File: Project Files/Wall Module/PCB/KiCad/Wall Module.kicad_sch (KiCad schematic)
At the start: 15 parts, among them J1 Conn_02x03_Top_Bottom (C65114), J2 Screw_Terminal_01x04 (C280261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, K1 SANYOU_SRD_Form_C (C35449), K2 SANYOU_SRD_Form_C (C35449), Q1 MMBT3904 (C20526), Q2 MMBT3904 (C20526), U1 AMS1117-3.3 (C173386)

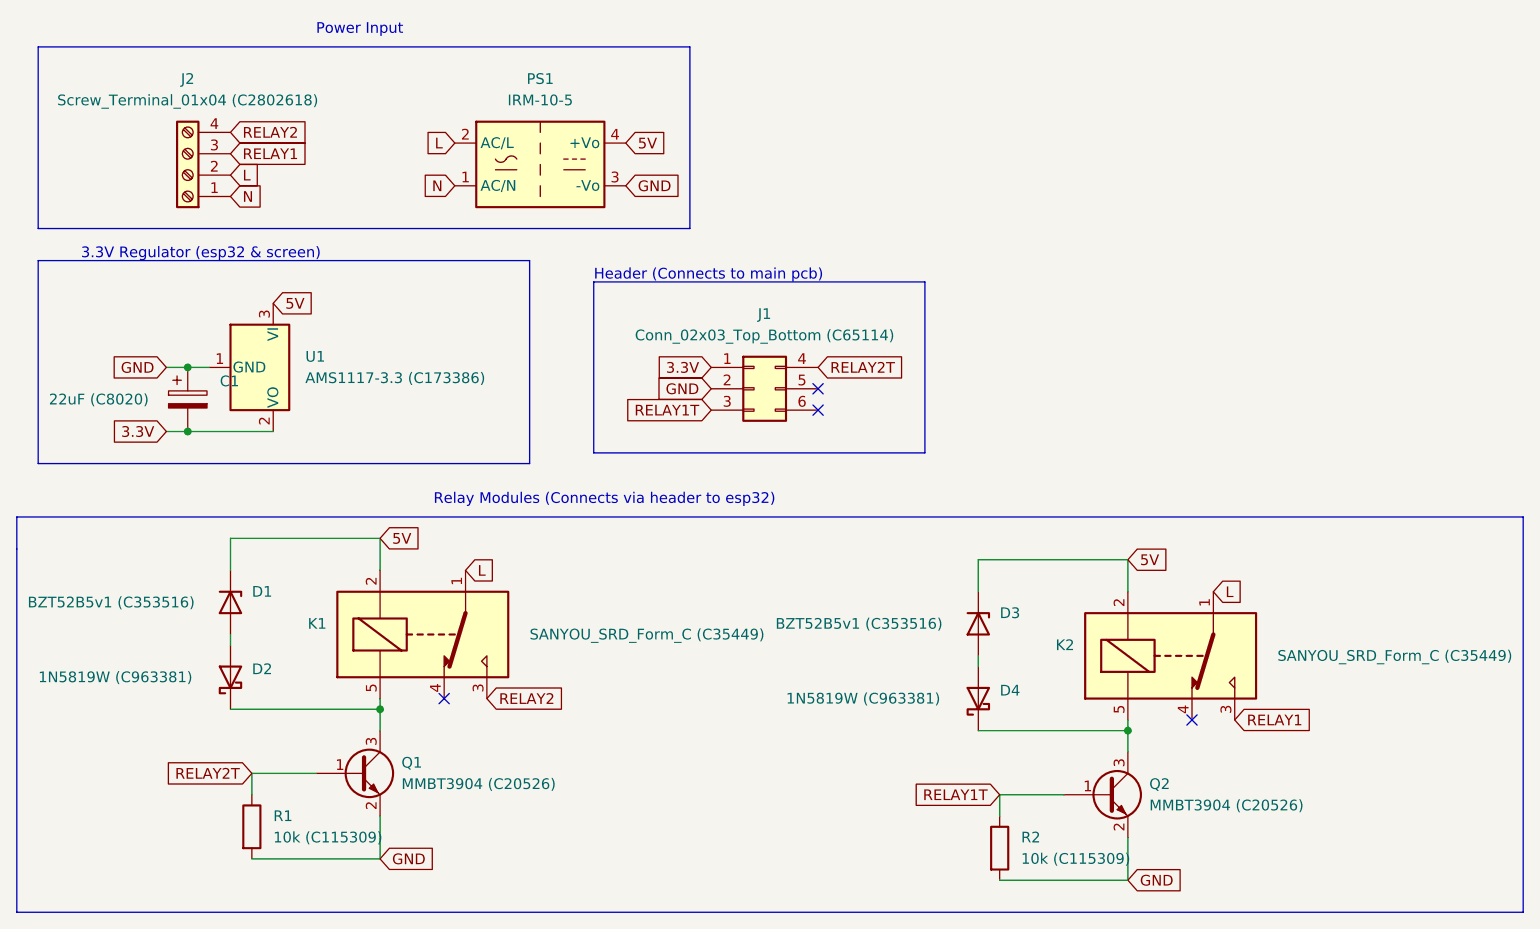
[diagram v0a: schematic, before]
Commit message: Updated PCB to fix several issues Wall Module: Fixed relay flyback diodes pointing in the wrong direction.
Screen PCB:
Fixed display LED resistors to be a more suitable value.
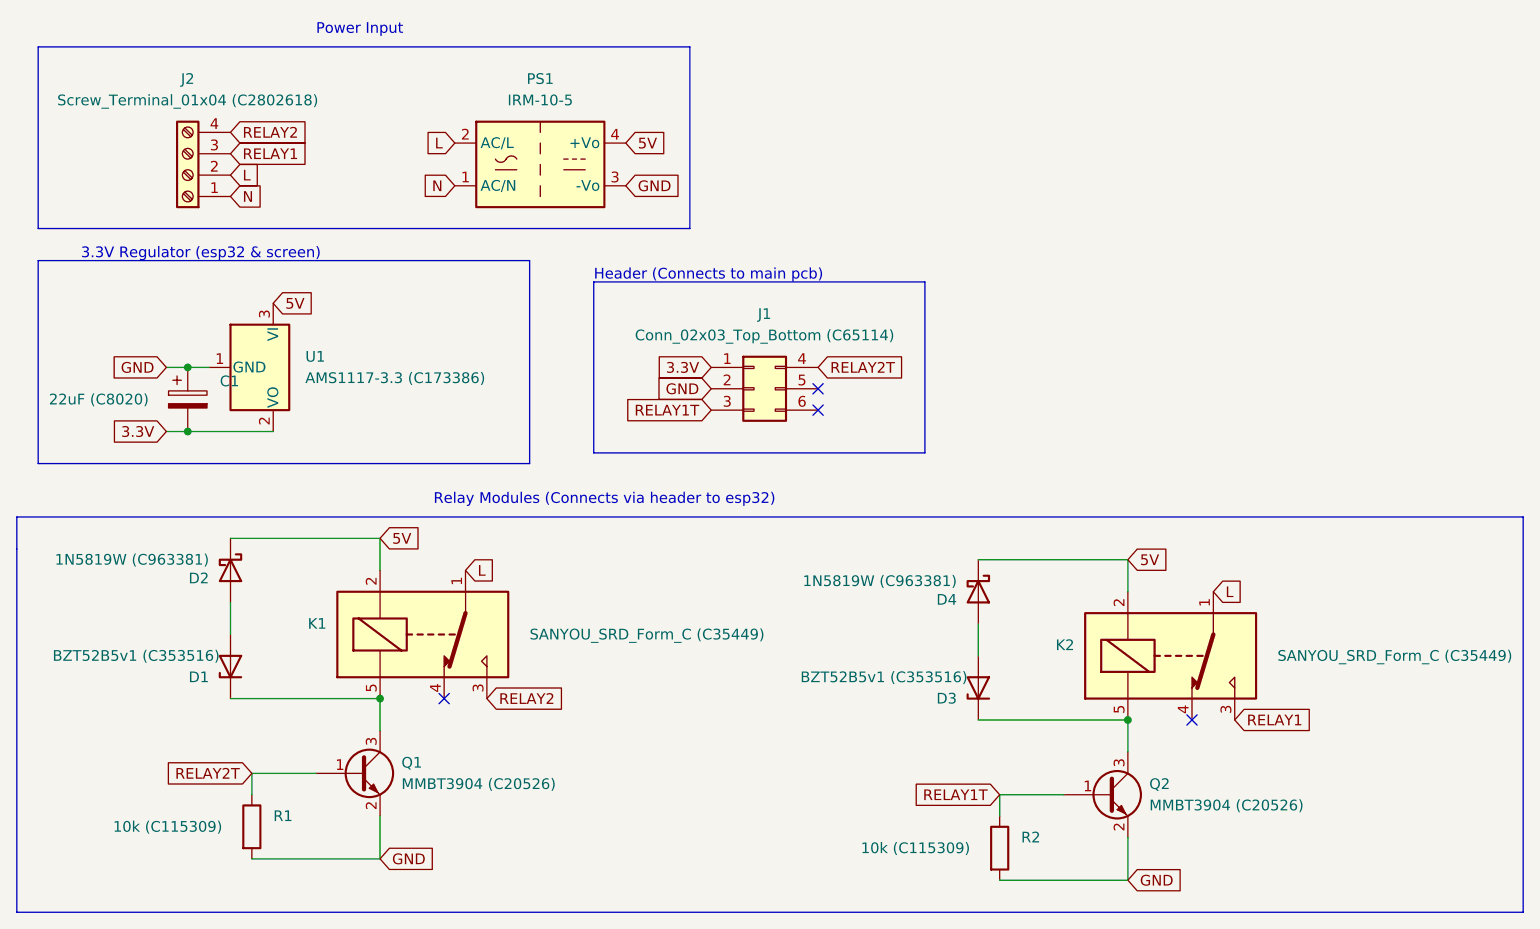
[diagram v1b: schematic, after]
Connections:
- net 5V: now also D2.1 (K), D4.1 (K); no longer D1.1 (K), D3.1 (K)
- net at K1.5, Q1.3 (C): now also D1.1 (K); no longer D2.1 (K)
- net at K2.5, Q2.3 (C): now also D3.1 (K); no longer D4.1 (K)
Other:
- moved on the sheet: D1, D2, D3, D4
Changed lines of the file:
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@@
 (kicad_sch (version 20211123) (generator eeschema)
   (paper "A4")
+  (junction (at 147.32 104.14) (diameter 0) (color 0 0 0 0)
+  )
+  (junction (at 58.42 101.6) (diameter 0) (color 0 0 0 0)
+  )
   (junction (at 35.56 69.85) (diameter 0) (color 0 0 0 0)
-  )
-  (junction (at 147.32 105.41) (diameter 0) (color 0 0 0 0)
-  )
-  (junction (at 58.42 102.87) (diameter 0) (color 0 0 0 0)
   )
   (junction (at 35.56 62.23) (diameter 0) (color 0 0 0 0)
@@
   (no_connect (at 66.04 101.6))
   (no_connect (at 110.49 64.77))
-  (wire (pts (xy 40.64 86.36) (xy 40.64 82.55))
-    (stroke (width 0) (type default) (color 0 0 0 0))
-  )
   (polyline (pts (xy 83.82 72.39) (xy 123.19 72.39))
     (stroke (width 0) (type default) (color 0 0 0 0))
@@
     (stroke (width 0) (type default) (color 0 0 0 0))
   )
-  (wire (pts (xy 147.32 105.41) (xy 147.32 104.14))
+  (wire (pts (xy 129.54 104.14) (xy 147.32 104.14))
+    (stroke (width 0) (type default) (color 0 0 0 0))
+  )
+  (wire (pts (xy 40.64 101.6) (xy 58.42 101.6))
     (stroke (width 0) (type default) (color 0 0 0 0))
   )
@@
     (stroke (width 0) (type default) (color 0 0 0 0))
   )
-  (wire (pts (xy 58.42 102.87) (xy 58.42 101.6))
-    (stroke (width 0) (type default) (color 0 0 0 0))
-  )
-  (wire (pts (xy 129.54 88.9) (xy 129.54 85.09))
+  (wire (pts (xy 58.42 101.6) (xy 58.42 105.41))
+    (stroke (width 0) (type default) (color 0 0 0 0))
+  )
+  (wire (pts (xy 40.64 90.17) (xy 40.64 93.98))
     (stroke (width 0) (type default) (color 0 0 0 0))
   )
@@
     (stroke (width 0) (type default) (color 0 0 0 0))
   )
-  (wire (pts (xy 58.42 105.41) (xy 58.42 102.87))
-    (stroke (width 0) (type default) (color 0 0 0 0))
-  )
   (wire (pts (xy 139.7 113.03) (xy 132.08 113.03))
     (stroke (width 0) (type default) (color 0 0 0 0))
@@
     (stroke (width 0) (type default) (color 0 0 0 0))
   )
+  (wire (pts (xy 129.54 92.71) (xy 129.54 96.52))
+    (stroke (width 0) (type default) (color 0 0 0 0))
+  )
   (polyline (pts (xy 15.24 127) (xy 194.31 127))
     (stroke (width 0) (type default) (color 0 0 0 0))
   )
-  (wire (pts (xy 147.32 107.95) (xy 147.32 105.41))
+  (wire (pts (xy 147.32 104.14) (xy 147.32 107.95))
     (stroke (width 0) (type default) (color 0 0 0 0))
   )
@@
     (stroke (width 0) (type default) (color 0 0 0 0))
   )
-  (wire (pts (xy 40.64 102.87) (xy 58.42 102.87))
-    (stroke (width 0) (type default) (color 0 0 0 0))
-  )
-  (wire (pts (xy 129.54 105.41) (xy 147.32 105.41))
-    (stroke (width 0) (type default) (color 0 0 0 0))
-  )
   (wire (pts (xy 43.18 120.65) (xy 58.42 120.65))
     (stroke (width 0) (type default) (color 0 0 0 0))
@@
     (stroke (width 0) (type default) (color 0 0 0 0))
   )
-  (wire (pts (xy 40.64 93.98) (xy 40.64 95.25))
-    (stroke (width 0) (type default) (color 0 0 0 0))
-  )
   (polyline (pts (xy 83.82 52.07) (xy 83.82 72.39))
     (stroke (width 0) (type default) (color 0 0 0 0))
@@
   )
   (polyline (pts (xy 194.31 80.01) (xy 15.24 80.01))
-    (stroke (width 0) (type default) (color 0 0 0 0))
-  )
-  (wire (pts (xy 129.54 96.52) (xy 129.54 97.79))
     (stroke (width 0) (type default) (color 0 0 0 0))
   )
@@
   )
   (symbol (lib_id "Device:R") (at 132.08 119.38 0) (unit 1)
-    (in_bom yes) (on_board yes) (fields_autoplaced)
+    (in_bom yes) (on_board yes)
     (property "Reference" "R2" (id 0) (at 134.62 118.1099 0)
       (effects (font (size 1.27 1.27)) (justify left))
     )
-    (property "Value" "10k (C115309)" (id 1) (at 134.62 120.6499 0)
+    (property "Value" "10k (C115309)" (id 1) (at 115.57 119.38 0)
       (effects (font (size 1.27 1.27)) (justify left))
     )
@@
   )
   (symbol (lib_id "Device:R") (at 43.18 116.84 0) (unit 1)
-    (in_bom yes) (on_board yes) (fields_autoplaced)
+    (in_bom yes) (on_board yes)
     (property "Reference" "R1" (id 0) (at 45.72 115.5699 0)
       (effects (font (size 1.27 1.27)) (justify left))
     )
-    (property "Value" "10k (C115309)" (id 1) (at 45.72 118.1099 0)
+    (property "Value" "10k (C115309)" (id 1) (at 26.67 116.84 0)
       (effects (font (size 1.27 1.27)) (justify left))
     )
@@
     (pin "2")
   )
-  (symbol (lib_id "Diode:1N5819") (at 40.64 99.06 90) (unit 1)
-    (in_bom yes) (on_board yes)
-    (property "Reference" "D2" (id 0) (at 43.18 98.1074 90)
-      (effects (font (size 1.27 1.27)) (justify right))
-    )
-    (property "Value" "1N5819W (C963381)" (id 1) (at 17.78 99.06 90)
-      (effects (font (size 1.27 1.27)) (justify right))
-    )
-    (property "Footprint" "Diode_SMD:D_SOD-123" (id 2) (at 45.085 99.06 0)
-      (effects (font (size 1.27 1.27)) hide)
-    )
-    (property "Datasheet" "http://www.vishay.com/docs/88525/1n5817.pdf" (id 3) (at 40.64 99.06 0)
+  (symbol (lib_id "Diode:1N5819") (at 40.64 86.36 270) (unit 1)
+    (in_bom yes) (on_board yes)
+    (property "Reference" "D2" (id 0) (at 38.1 87.3126 90)
+      (effects (font (size 1.27 1.27)) (justify right))
+    )
+    (property "Value" "1N5819W (C963381)" (id 1) (at 38.1 85.09 90)
+      (effects (font (size 1.27 1.27)) (justify right))
+    )
+    (property "Footprint" "Diode_SMD:D_SOD-123" (id 2) (at 36.195 86.36 0)
+      (effects (font (size 1.27 1.27)) hide)
+    )
+    (property "Datasheet" "http://www.vishay.com/docs/88525/1n5817.pdf" (id 3) (at 40.64 86.36 0)
       (effects (font (size 1.27 1.27)) hide)
     )
@@
     (pin "5")
   )
-  (symbol (lib_id "Diode:1N5819") (at 129.54 101.6 90) (unit 1)
-    (in_bom yes) (on_board yes)
-    (property "Reference" "D4" (id 0) (at 132.08 100.6474 90)
-      (effects (font (size 1.27 1.27)) (justify right))
-    )
-    (property "Value" "1N5819W (C963381)" (id 1) (at 106.68 101.6 90)
-      (effects (font (size 1.27 1.27)) (justify right))
-    )
-    (property "Footprint" "Diode_SMD:D_SOD-123" (id 2) (at 133.985 101.6 0)
-      (effects (font (size 1.27 1.27)) hide)
-    )
-    (property "Datasheet" "http://www.vishay.com/docs/88525/1n5817.pdf" (id 3) (at 129.54 101.6 0)
+  (symbol (lib_id "Diode:1N5819") (at 129.54 88.9 270) (unit 1)
+    (in_bom yes) (on_board yes)
+    (property "Reference" "D4" (id 0) (at 127 89.8526 90)
+      (effects (font (size 1.27 1.27)) (justify right))
+    )
+    (property "Value" "1N5819W (C963381)" (id 1) (at 127 87.63 90)
+      (effects (font (size 1.27 1.27)) (justify right))
+    )
+    (property "Footprint" "Diode_SMD:D_SOD-123" (id 2) (at 125.095 88.9 0)
+      (effects (font (size 1.27 1.27)) hide)
+    )
+    (property "Datasheet" "http://www.vishay.com/docs/88525/1n5817.pdf" (id 3) (at 129.54 88.9 0)
       (effects (font (size 1.27 1.27)) hide)
     )
@@
     (pin "6")
   )
-  (symbol (lib_id "Diode:BZT52Bxx") (at 40.64 90.17 270) (unit 1)
-    (in_bom yes) (on_board yes)
-    (property "Reference" "D1" (id 0) (at 43.18 88.8999 90)
-      (effects (font (size 1.27 1.27)) (justify left))
-    )
-    (property "Value" "BZT52B5v1 (C353516)" (id 1) (at 16.51 90.17 90)
-      (effects (font (size 1.27 1.27)) (justify left))
-    )
-    (property "Footprint" "Diode_SMD:D_SOD-123" (id 2) (at 36.195 90.17 0)
-      (effects (font (size 1.27 1.27)) hide)
-    )
-    (property "Datasheet" "https://diotec.com/tl_files/diotec/files/pdf/datasheets/bzt52b2v4.pdf" (id 3) (at 40.64 90.17 0)
+  (symbol (lib_id "Diode:BZT52Bxx") (at 40.64 97.79 90) (unit 1)
+    (in_bom yes) (on_board yes)
+    (property "Reference" "D1" (id 0) (at 38.1 99.0601 90)
+      (effects (font (size 1.27 1.27)) (justify left))
+    )
+    (property "Value" "BZT52B5v1 (C353516)" (id 1) (at 39.37 96.52 90)
+      (effects (font (size 1.27 1.27)) (justify left))
+    )
+    (property "Footprint" "Diode_SMD:D_SOD-123" (id 2) (at 45.085 97.79 0)
+      (effects (font (size 1.27 1.27)) hide)
+    )
+    (property "Datasheet" "https://diotec.com/tl_files/diotec/files/pdf/datasheets/bzt52b2v4.pdf" (id 3) (at 40.64 97.79 0)
       (effects (font (size 1.27 1.27)) hide)
     )
@@
     (pin "2")
   )
-  (symbol (lib_id "Diode:BZT52Bxx") (at 129.54 92.71 270) (unit 1)
-    (in_bom yes) (on_board yes)
-    (property "Reference" "D3" (id 0) (at 132.08 91.4399 90)
-      (effects (font (size 1.27 1.27)) (justify left))
-    )
-    (property "Value" "BZT52B5v1 (C353516)" (id 1) (at 105.41 92.71 90)
-      (effects (font (size 1.27 1.27)) (justify left))
-    )
-    (property "Footprint" "Diode_SMD:D_SOD-123" (id 2) (at 125.095 92.71 0)
-      (effects (font (size 1.27 1.27)) hide)
-    )
-    (property "Datasheet" "https://diotec.com/tl_files/diotec/files/pdf/datasheets/bzt52b2v4.pdf" (id 3) (at 129.54 92.71 0)
-      (effects (font (size 1.27 1.27)) hide)
-    )
+  (symbol (lib_id "Diode:BZT52Bxx") (at 129.54 100.33 90) (unit 1)
+    (in_bom yes) (on_board yes)
+    (property "Reference" "D3" (id 0) (at 127 101.6001 90)
+      (effects (font (size 1.27 1.27)) (justify left))
+    )
+    (property "Value" "BZT52B5v1 (C353516)" (id 1) (at 128.27 99.06 90)
+      (effects (font (size 1.27 1.27)) (justify left))
+    )
+    (property "Footprint" "Diode_SMD:D_SOD-123" (id 2) (at 133.985 100.33 0)
+      (effects (font (size 1.27 1.27)) hide)
+    )
+    (property "Datasheet" "https://diotec.com/tl_files/diotec/files/pdf/datasheets/bzt52b2v4.pdf" (id 3) (at 129.54 100.33 0)
+      (effects (font (size 1.27 1.27)) hide)
+    )
